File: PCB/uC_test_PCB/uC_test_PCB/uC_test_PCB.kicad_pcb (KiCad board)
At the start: 2 copper layers, 105.8 x 15 mm, 35 parts, among them J1 781710004, J3 SM03B-SRSS-TB, J4 SM03B-SRSS-TB, Q3 DMG2305, SW101 KMR2, SW102 KMR2, U1 Core52840, U2 AP2112(3.3V), U3 MCP73831T-2ACI/OT, X3 JSTPH

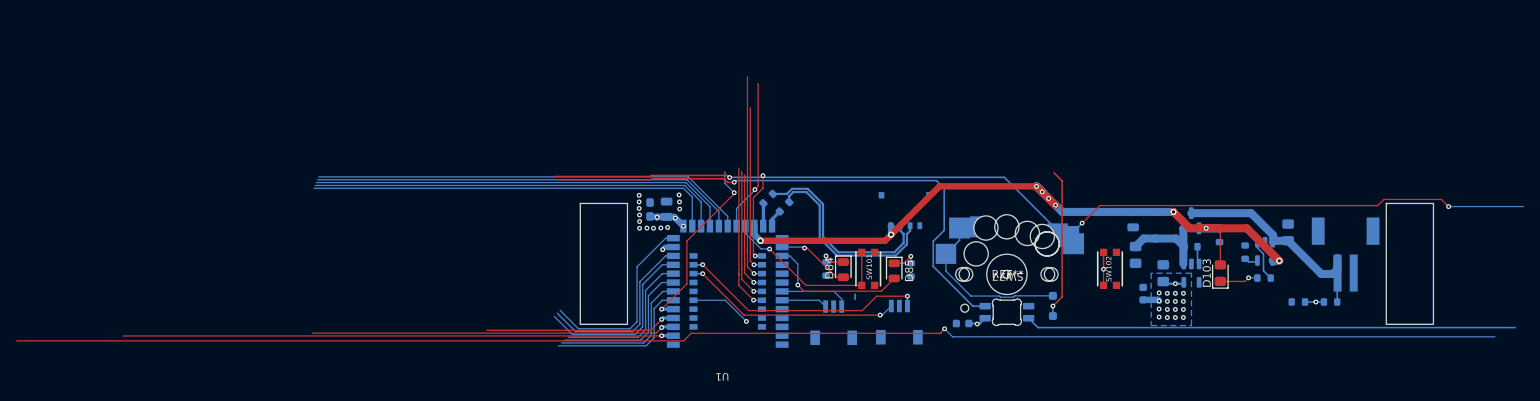
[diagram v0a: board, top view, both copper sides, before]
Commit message: uC test pcb done
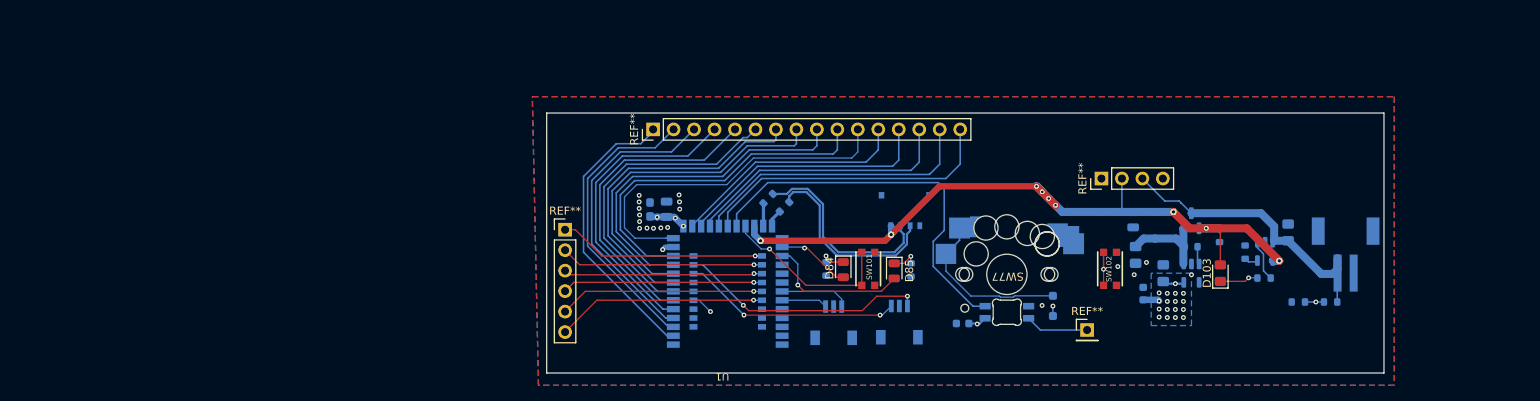
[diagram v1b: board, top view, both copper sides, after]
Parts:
- removed the REF** at (160.2, 118.3)
- added REF**: PinHeader_1x06_P2.54mm_Vertical, Connector_PinHeader_2.54mm:PinHeader_1x06_P2.54mm_Vertical, F.Cu at (105.4, 112.8)
- added REF**: PinHeader_1x04_P2.54mm_Vertical, Connector_PinHeader_2.54mm:PinHeader_1x04_P2.54mm_Vertical, F.Cu at (172.0, 106.4)
- added REF**: PinHeader_1x01_P2.54mm_Vertical, Connector_PinHeader_2.54mm:PinHeader_1x01_P2.54mm_Vertical, F.Cu at (170.2, 125.2)
- added REF**: PinHeader_1x16_P2.54mm_Vertical, Connector_PinHeader_2.54mm:PinHeader_1x16_P2.54mm_Vertical, F.Cu at (116.3, 100.3)
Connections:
- C3 pad 1: (no net) -> GND
- C3 pad 2: (no net) -> 3v3
- C4 pad 1: (no net) -> GND
- C4 pad 2: (no net) -> 3v3
- C5 pad 1: (no net) -> GND
- C5 pad 2: (no net) -> 3v3
- C6 pad 1: (no net) -> GND
- C7 pad 1: (no net) -> GND
- C8 pad 1: (no net) -> GND
- C8 pad 2: (no net) -> 3v3
- C87 pad 1: (no net) -> 3v3
- C87 pad 2: (no net) -> GND
- C9 pad 1: (no net) -> GND
- J1 pad 4: (no net) -> GND
- J1 pad 5: (no net) -> GND
- J1 pad 6: (no net) -> GND
- J3 pad 2: (no net) -> GND
- J3 pad 4: (no net) -> GND
- J3 pad 5: (no net) -> GND
- J4 pad 2: (no net) -> GND
- J4 pad 4: (no net) -> GND
- J4 pad 5: (no net) -> GND
- R2 pad 2: (no net) -> GND
- R4 pad 2: (no net) -> GND
- R5 pad 2: (no net) -> GND
- R7 pad 2: (no net) -> GND
- R9 pad 2: (no net) -> GND
- SW102 pad A: (no net) -> GND
- SW102 pad A': (no net) -> GND
- SW77 pad 4: (no net) -> 3v3
- SW77 pad 6: (no net) -> GND
- U1 pad 1: (no net) -> GND
- U1 pad 32: (no net) -> GND
- U1 pad 44: (no net) -> GND
- U1 pad 55: (no net) -> 3v3
- U2 pad 2: (no net) -> GND
- U2 pad 5: (no net) -> 3v3
- U3 pad 2: (no net) -> GND
- X3 pad 1: (no net) -> GND
- X3 pad NC1: (no net) -> GND
- X3 pad NC2: (no net) -> GND
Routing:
- net (no net): track 1521.5 -> 1331.9 mm, vias 76 -> 30
- net 3v3: track 0.00 -> 11.5 mm, vias 0 -> 21
- net GND: vias 0 -> 18
- added copper zone on B.Cu, net 3v3
- added copper zone on In1.Cu, net 3v3
- added copper zone on B.Cu, net GND
- added copper zone on F.Cu, net GND
- added copper zone on In2.Cu, net GND
- removed copper zone on B.Cu, net (none)
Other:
- board size 105.8 x 15 mm -> 103.9 x 32.3 mm
- copper layers 2 -> 4

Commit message: Test pcb
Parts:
- moved X3 16.3 mm to (190.2, 103.5)
- moved R12 6.22 mm to (194.2, 121.8)
- moved R9 6.22 mm to (190.2, 121.8)
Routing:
- net (no net): track 1331.9 -> 1321.9 mm
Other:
- board size 103.9 x 32.3 mm -> 93.9 x 32.3 mm
- board text added: "Design by MW"
